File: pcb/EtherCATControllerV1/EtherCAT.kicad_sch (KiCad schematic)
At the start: 45 parts, among them U7 LAN9252I/ML, U9 24FC512-I/SN, Y2 25 MHz, 25ppm

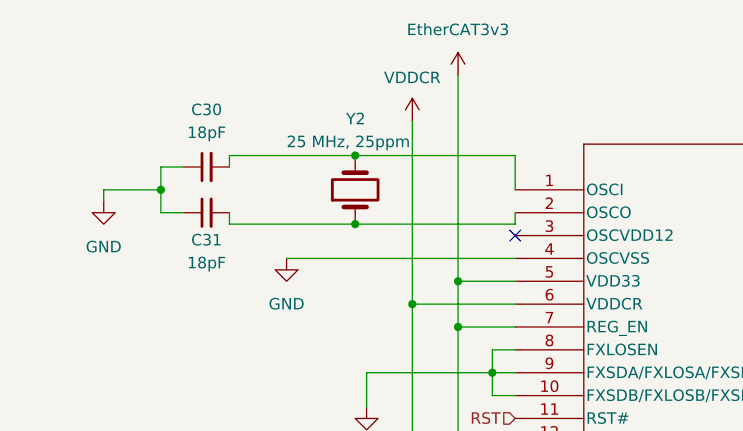
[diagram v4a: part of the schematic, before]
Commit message: Added more BOM items
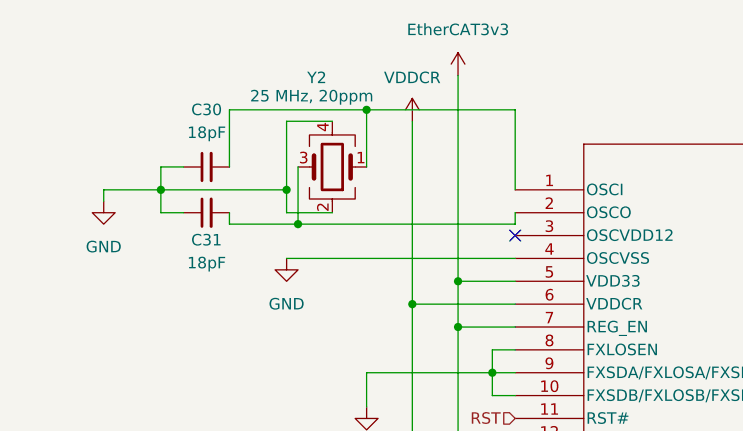
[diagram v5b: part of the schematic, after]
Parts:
- removed Y2: 25 MHz, 25ppm, symbol Device:Crystal
- added Y2: 25 MHz, 20ppm, symbol Device:Crystal_GND24
- U7: LCSC Part Number (none) -> C2758355
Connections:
- net GND: now also Y2.2, Y2.4
- net at C30.2, U7.1 (OSCI): now also Y2.1
- net at C31.2, U7.2 (OSCO): now also Y2.3
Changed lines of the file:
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@@
 	)
 	(junction
-		(at 157.48 194.31)
+		(at 53.34 49.53)
 		(diameter 0)
 		(color 0 0 0 0)
 	)
 	(junction
-		(at 331.47 177.8)
+		(at 157.48 194.31)
 		(diameter 0)
 		(color 0 0 0 0)
 	)
 	(junction
-		(at 60.96 45.72)
+		(at 331.47 177.8)
 		(diameter 0)
 		(color 0 0 0 0)
@@
 	)
 	(junction
-		(at 60.96 53.34)
-		(diameter 0)
-		(color 0 0 0 0)
-	)
-	(junction
 		(at 119.38 204.47)
 		(diameter 0)
@@
 	)
 	(junction
+		(at 62.23 40.64)
+		(diameter 0)
+		(color 0 0 0 0)
+	)
+	(junction
 		(at 323.85 193.04)
 		(diameter 0)
@@
 	)
 	(junction
+		(at 54.61 53.34)
+		(diameter 0)
+		(color 0 0 0 0)
+	)
+	(junction
 		(at 132.08 162.56)
 		(diameter 0)
@@
 	(wire
 		(pts
-			(xy 46.99 45.72) (xy 46.99 46.99)
+			(xy 46.99 40.64) (xy 46.99 46.99)
+		)
+		(stroke
+			(width 0)
+			(type default)
+		)
+	)
+	(wire
+		(pts
+			(xy 54.61 53.34) (xy 78.74 53.34)
 		)
 		(stroke
@@
 	(wire
 		(pts
+			(xy 39.37 49.53) (xy 53.34 49.53)
+		)
+		(stroke
+			(width 0)
+			(type default)
+		)
+	)
+	(wire
+		(pts
 			(xy 292.1 72.39) (xy 317.5 72.39)
 		)
@@
 	(wire
 		(pts
+			(xy 62.23 40.64) (xy 62.23 46.99)
+		)
+		(stroke
+			(width 0)
+			(type default)
+		)
+	)
+	(wire
+		(pts
 			(xy 144.78 148.59) (xy 144.78 149.86)
 		)
@@
 	(wire
 		(pts
+			(xy 62.23 40.64) (xy 78.74 40.64)
+		)
+		(stroke
+			(width 0)
+			(type default)
+		)
+	)
+	(wire
+		(pts
 			(xy 119.38 198.12) (xy 119.38 194.31)
 		)
@@
 	(wire
 		(pts
-			(xy 46.99 53.34) (xy 60.96 53.34)
+			(xy 46.99 53.34) (xy 54.61 53.34)
 		)
 		(stroke
@@
 	(wire
 		(pts
+			(xy 58.42 52.07) (xy 53.34 52.07)
+		)
+		(stroke
+			(width 0)
+			(type default)
+		)
+	)
+	(wire
+		(pts
+			(xy 58.42 41.91) (xy 53.34 41.91)
+		)
+		(stroke
+			(width 0)
+			(type default)
+		)
+	)
+	(wire
+		(pts
 			(xy 292.1 67.31) (xy 312.42 67.31)
 		)
@@
 	(wire
 		(pts
-			(xy 78.74 45.72) (xy 78.74 49.53)
+			(xy 78.74 40.64) (xy 78.74 49.53)
 		)
 		(stroke
@@
 	(wire
 		(pts
-			(xy 60.96 53.34) (xy 78.74 53.34)
-		)
-		(stroke
-			(width 0)
-			(type default)
-		)
-	)
-	(wire
-		(pts
 			(xy 157.48 167.64) (xy 157.48 171.45)
 		)
@@
 	(wire
 		(pts
+			(xy 54.61 46.99) (xy 54.61 53.34)
+		)
+		(stroke
+			(width 0)
+			(type default)
+		)
+	)
+	(wire
+		(pts
 			(xy 55.88 176.53) (xy 55.88 177.8)
 		)
@@
 	(wire
 		(pts
+			(xy 53.34 52.07) (xy 53.34 49.53)
+		)
+		(stroke
+			(width 0)
+			(type default)
+		)
+	)
+	(wire
+		(pts
 			(xy 168.91 194.31) (xy 168.91 198.12)
 		)
@@
 	(wire
 		(pts
-			(xy 46.99 45.72) (xy 60.96 45.72)
+			(xy 46.99 40.64) (xy 62.23 40.64)
 		)
 		(stroke
@@
 	(wire
 		(pts
-			(xy 293.37 102.87) (xy 292.1 102.87)
+			(xy 53.34 41.91) (xy 53.34 49.53)
 		)
 		(stroke
@@
 	(wire
 		(pts
-			(xy 60.96 45.72) (xy 78.74 45.72)
+			(xy 293.37 102.87) (xy 292.1 102.87)
 		)
 		(stroke
@@
 			)
 		)
-		(property "LCSC Part Number" ""
-			(at 78.74 49.53 0)
-			(effects
-				(font
-					(size 1.27 1.27)
-				)
-				(hide yes)
-			)
-		)
-		(property "Field-1" ""
+		(property "LCSC Part Number" "C2758355"
 			(at 78.74 49.53 0)
 			(effects
@@
 	)
 	(symbol
+		(lib_id "Device:Crystal_GND24")
+		(at 58.42 46.99 180)
+		(unit 1)
+		(exclude_from_sim no)
+		(in_bom yes)
+		(on_board yes)
+		(dnp no)
+		(property "Reference" "Y2"
+			(at 55.626 37.084 0)
+			(effects
+				(font
+					(size 1.27 1.27)
+				)
+				(justify right)
+			)
+		)
+		(property "Value" "25 MHz, 20ppm"
+			(at 49.276 39.1159 0)
+			(effects
+				(font
+					(size 1.27 1.27)
+				)
+				(justify right)
+			)
+		)
+		(property "Footprint" ""
+			(at 58.42 46.99 0)
+			(effects
+				(font
+					(size 1.27 1.27)
+				)
+				(hide yes)
+			)
+		)
+		(property "Datasheet" "~"
+			(at 58.42 46.99 0)
+			(effects
+				(font
+					(size 1.27 1.27)
+				)
+				(hide yes)
+			)
+		)
+		(property "Description" "Four pin crystal, GND on pins 2 and 4"
+			(at 58.42 46.99 0)
+			(effects
+				(font
+					(size 1.27 1.27)
+				)
+				(hide yes)
+			)
+		)
+		(property "LCSC Part Number" "C179643"
+			(at 58.42 46.99 0)
+			(effects
+				(font
+					(size 1.27 1.27)
+				)
+				(hide yes)
+			)
+		)
+		(pin "2"
+		)
+		(pin "1"
+		)
+		(pin "4"
+		)
+		(pin "3"
+		)
+		(instances
+			(project "EtherCATControllerV1"
+				(path "/4c927f80-855d-490a-80b2-e5c55283621a/750b7685-89f9-49f1-8425-82b30a74de18"
+					(reference "Y2")
+					(unit 1)
+				)
+			)
+		)
+	)
+	(symbol
 		(lib_id "Device:C_Small")
 		(at 321.31 72.39 90)
@@
 					(unit 1)
 				)
-			)
-		)
-	)
-	(symbol
-		(lib_id "Device:Crystal")
-		(at 60.96 49.53 90)
-		(unit 1)
-		(exclude_from_sim no)
-		(in_bom yes)
-		(on_board yes)
-		(dnp no)
-		(property "Reference" "Y2"
-			(at 59.944 41.656 90)
-			(effects
-				(font
-					(size 1.27 1.27)
-				)
-				(justify right)
-			)
-		)
-		(property "Value" "25 MHz, 25ppm"
-			(at 53.34 44.1961 90)
-			(effects
-				(font
-					(size 1.27 1.27)
-				)
-				(justify right)
-			)
-		)
-		(property "Footprint" ""
-			(at 60.96 49.53 0)
-			(effects
-				(font
-					(size 1.27 1.27)
-				)
-				(hide yes)
-			)
-		)
-		(property "Datasheet" "~"
-			(at 60.96 49.53 0)
-			(effects
-				(font
-					(size 1.27 1.27)
-				)
-				(hide yes)
-			)
-		)
-		(property "Description" "Two pin crystal"
-			(at 60.96 49.53 0)
-			(effects
-				(font
-					(size 1.27 1.27)
-				)
-				(hide yes)
-			)
-		)
-		(pin "2"
-		)
-		(pin "1"
-		)
-		(instances
-			(project ""
-				(path "/4c927f80-855d-490a-80b2-e5c55283621a/750b7685-89f9-49f1-8425-82b30a74de18"
-					(reference "Y2")
-					(unit 1)
-				)
